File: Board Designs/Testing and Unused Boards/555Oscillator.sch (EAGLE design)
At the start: 8 parts

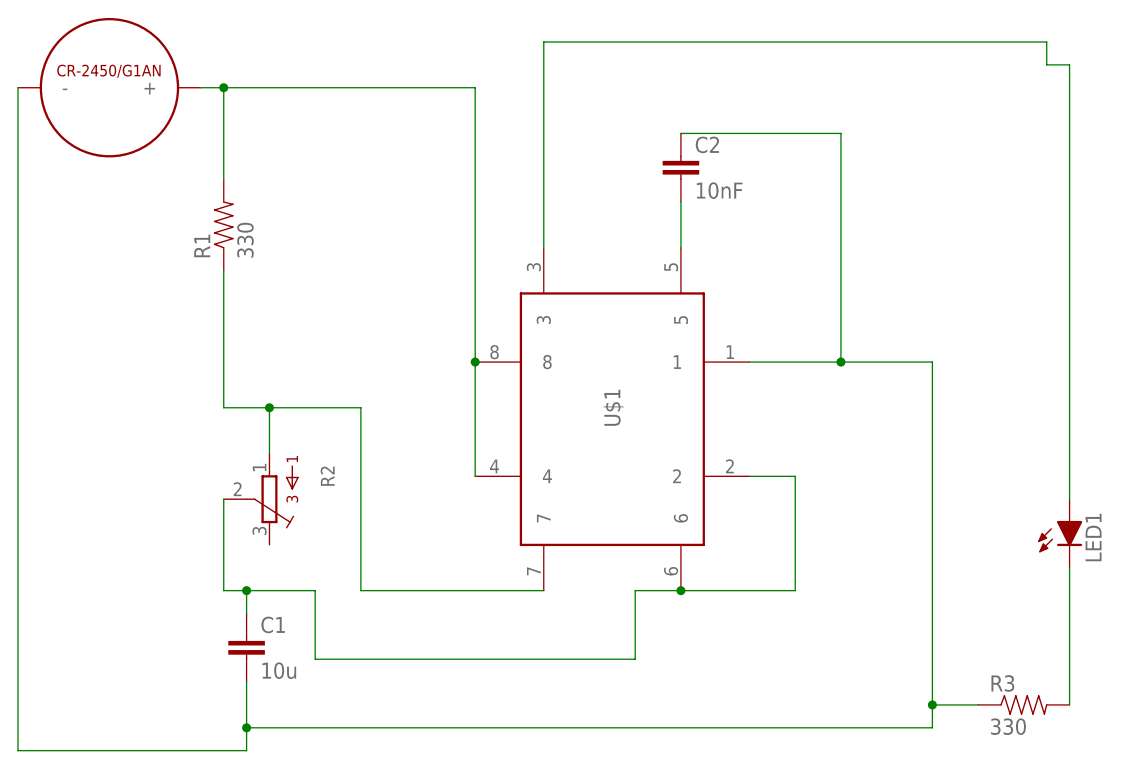
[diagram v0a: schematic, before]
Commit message: Modified solder test board for jlc
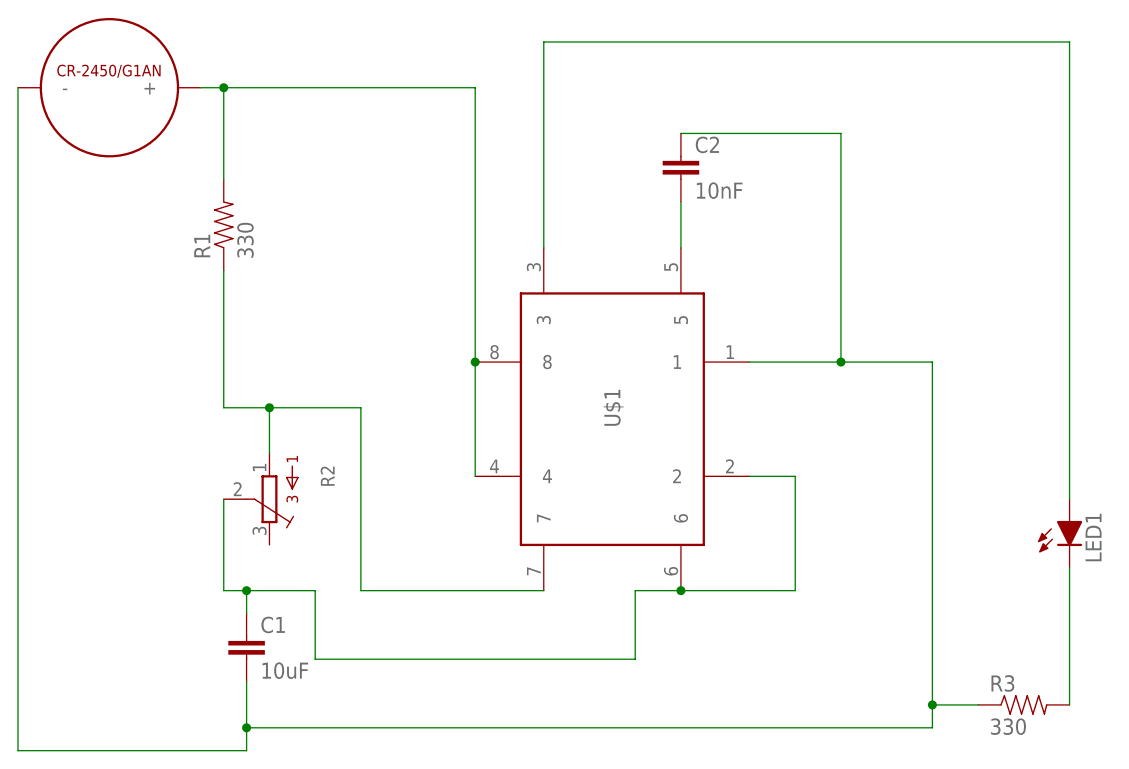
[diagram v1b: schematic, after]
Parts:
- C1: value 10u -> 10uF
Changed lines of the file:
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@@
 <?xml version="1.0" encoding="utf-8"?>
 <!DOCTYPE eagle SYSTEM "eagle.dtd">
-<eagle version="9.1.3">
+<eagle version="9.4.2">
 <drawing>
 <settings>
@@
 <part name="U$1" library="HyTechDevices" deviceset="555_TIMER" device=""/>
 <part name="U$2" library="HyTechDevices" deviceset="CR-2450/G1AN" device=""/>
-<part name="C1" library="HyTechDevices" deviceset="CAP" device="_" value="10u"/>
+<part name="C1" library="HyTechDevices" deviceset="CAP" device="_" value="10uF"/>
 <part name="C2" library="HyTechDevices" deviceset="CAP" device="_" value="10nF"/>
 <part name="R1" library="HyTechDevices" deviceset="RESISTOR" device="AXIAL-0.3" value="330"/>
@@
 </plain>
 <instances>
-<instance part="U$1" gate="G$1" x="58.42" y="43.18" rot="R90"/>
-<instance part="U$2" gate="G$1" x="-7.62" y="93.98" rot="R180"/>
-<instance part="C1" gate="G$1" x="7.62" y="30.48"/>
-<instance part="C2" gate="G$1" x="55.88" y="83.82"/>
-<instance part="R1" gate="G$1" x="5.08" y="78.74" rot="R90"/>
-<instance part="R2" gate="G$1" x="10.16" y="48.26" rot="R180"/>
-<instance part="LED1" gate="LED" x="99.06" y="45.72"/>
-<instance part="R3" gate="G$1" x="93.98" y="25.4"/>
+<instance part="U$1" gate="G$1" x="58.42" y="43.18" smashed="yes" rot="R90">
+<attribute name="NAME" x="48.26" y="58.42" size="1.778" layer="95" rot="R90" align="center"/>
+</instance>
+<instance part="U$2" gate="G$1" x="-7.62" y="93.98" smashed="yes" rot="R180"/>
+<instance part="C1" gate="G$1" x="7.62" y="30.48" smashed="yes">
+<attribute name="NAME" x="9.144" y="33.401" size="1.778" layer="95"/>
+<attribute name="VALUE" x="9.144" y="28.321" size="1.778" layer="96"/>
+</instance>
+<instance part="C2" gate="G$1" x="55.88" y="83.82" smashed="yes">
+<attribute name="NAME" x="57.404" y="86.741" size="1.778" layer="95"/>
+<attribute name="VALUE" x="57.404" y="81.661" size="1.778" layer="96"/>
+</instance>
+<instance part="R1" gate="G$1" x="5.08" y="78.74" smashed="yes" rot="R90">
+<attribute name="NAME" x="3.5814" y="74.93" size="1.778" layer="95" rot="R90"/>
+<attribute name="VALUE" x="8.382" y="74.93" size="1.778" layer="96" rot="R90"/>
+</instance>
+<instance part="R2" gate="G$1" x="10.16" y="48.26" smashed="yes" rot="R180">
+<attribute name="NAME" x="15.875" y="52.07" size="1.524" layer="95" ratio="10" rot="R270"/>
+<attribute name="VALUE" x="13.97" y="52.07" size="1.524" layer="96" ratio="10" rot="R270"/>
+</instance>
+<instance part="LED1" gate="LED" x="99.06" y="45.72" smashed="yes">
+<attribute name="NAME" x="102.616" y="41.148" size="1.778" layer="95" rot="R90"/>
+<attribute name="VALUE" x="104.775" y="41.148" size="1.778" layer="96" rot="R90"/>
+</instance>
+<instance part="R3" gate="G$1" x="93.98" y="25.4" smashed="yes">
+<attribute name="NAME" x="90.17" y="26.8986" size="1.778" layer="95"/>
+<attribute name="VALUE" x="90.17" y="22.098" size="1.778" layer="96"/>
+</instance>
 </instances>
 <busses>
@@
 <pinref part="U$1" gate="G$1" pin="3"/>
 <wire x1="40.64" y1="76.2" x2="40.64" y2="99.06" width="0.1524" layer="91"/>
-<wire x1="40.64" y1="99.06" x2="96.52" y2="99.06" width="0.1524" layer="91"/>
-<wire x1="96.52" y1="99.06" x2="96.52" y2="96.52" width="0.1524" layer="91"/>
+<wire x1="40.64" y1="99.06" x2="99.06" y2="99.06" width="0.1524" layer="91"/>
 <pinref part="LED1" gate="LED" pin="A"/>
-<wire x1="96.52" y1="96.52" x2="99.06" y2="96.52" width="0.1524" layer="91"/>
-<wire x1="99.06" y1="96.52" x2="99.06" y2="48.26" width="0.1524" layer="91"/>
-</segment>
-</net>
+<wire x1="99.06" y1="99.06" x2="99.06" y2="48.26" width="0.1524" layer="91"/>
+</segment>
+</net>
